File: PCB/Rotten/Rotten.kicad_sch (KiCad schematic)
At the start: 39 parts, among them J1 Jack-DC, J2 FOOTSWITCH, J3 JACK OUTPUT, J4 JACK INPUT, Q1 2N5458, U1 AS301

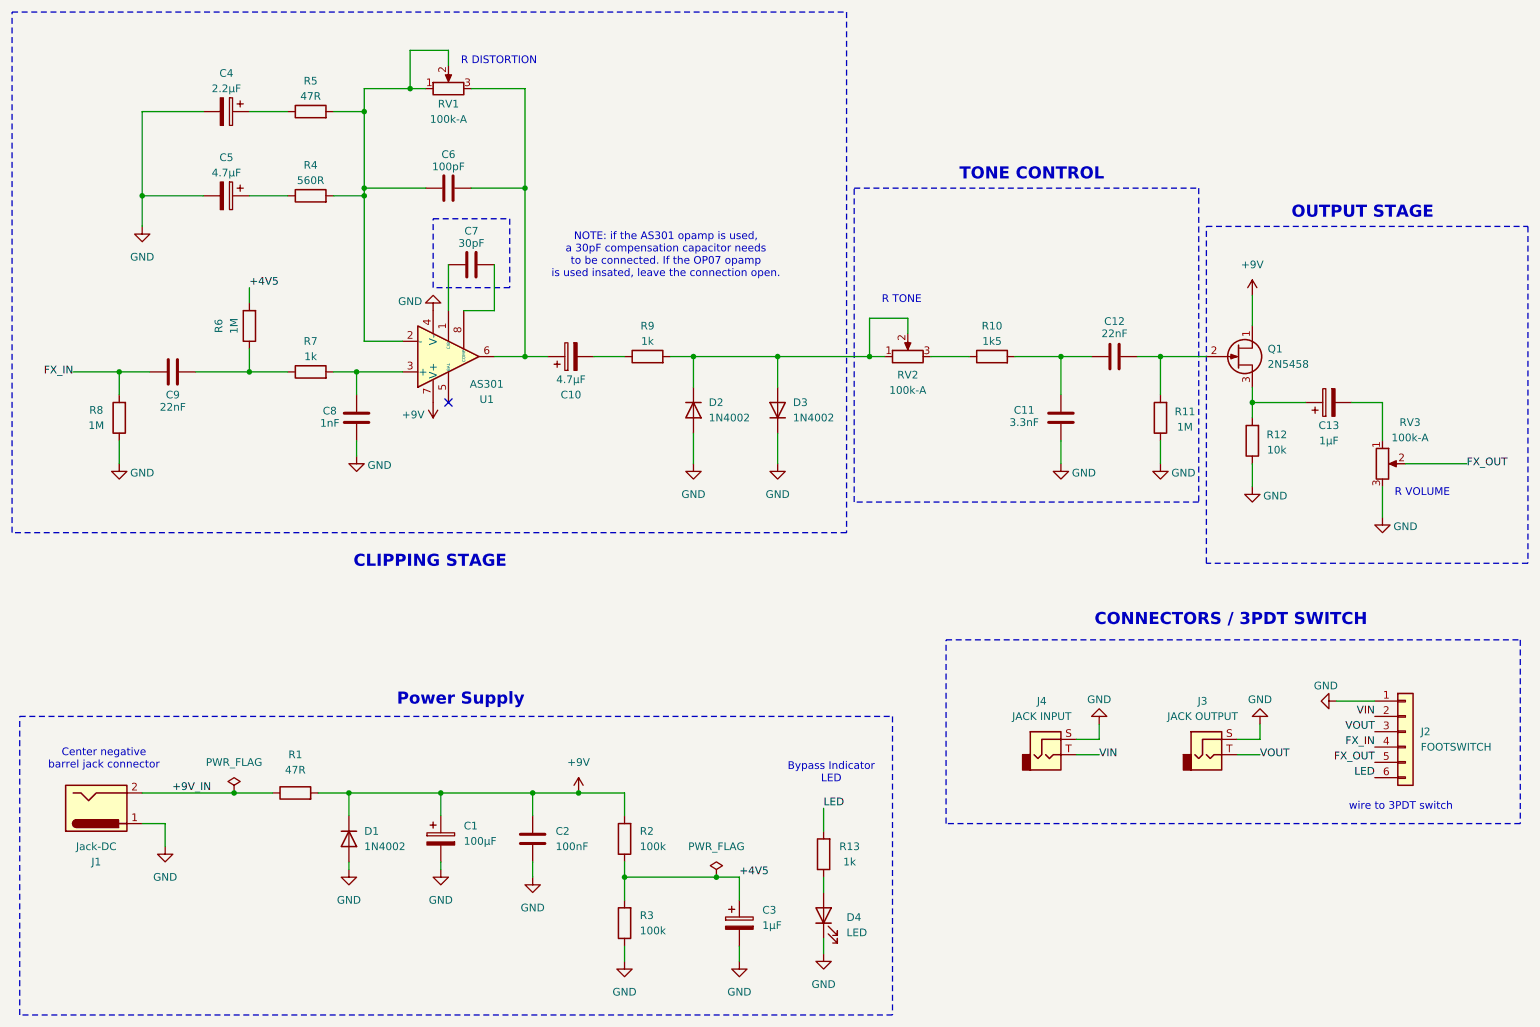
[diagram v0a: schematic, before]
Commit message: created rev1 layout and added images
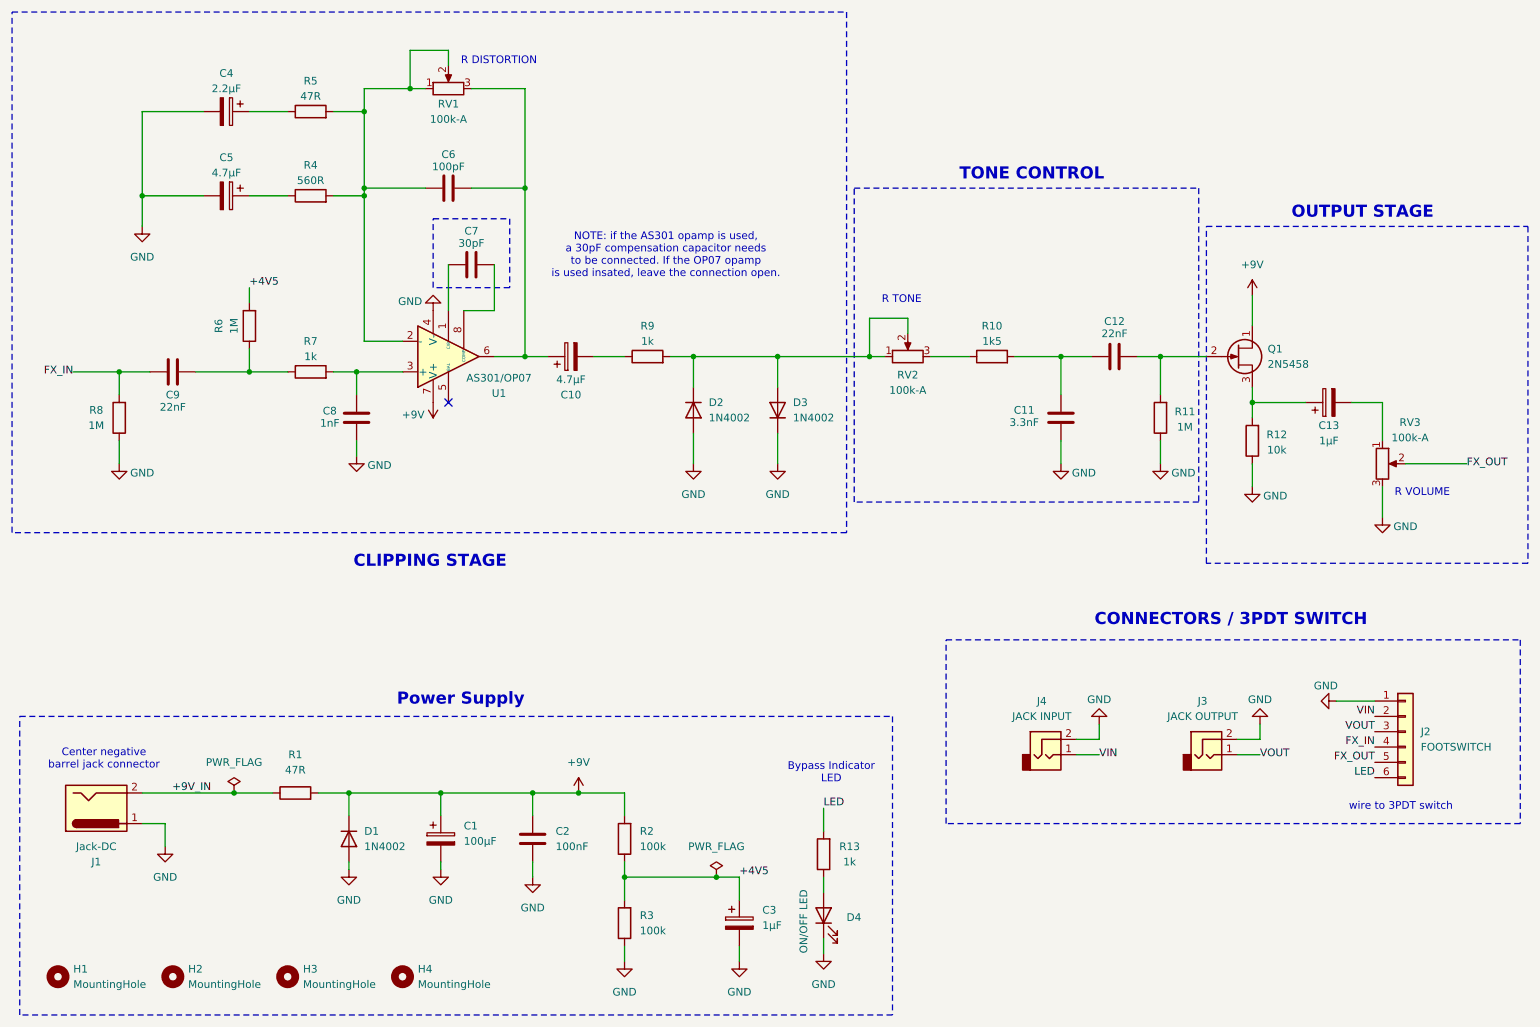
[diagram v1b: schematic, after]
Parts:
- added H1, H2, H3, H4: MountingHole, MountingHole:MountingHole_3.2mm_M3_DIN965, symbol Mechanical:MountingHole
- D4: value LED -> ON/OFF LED
- J1: footprint Connector_PinHeader_1.00mm:PinHeader_1x02_P1.00mm_Vertical -> Connector_PinHeader_2.54mm:PinHeader_1x02_P2.54mm_Vertical
- J3, J4: footprint TestPoint:TestPoint_2Pads_Pitch2.54mm_Drill0.8mm -> Connector_PinHeader_2.54mm:PinHeader_1x02_P2.54mm_Vertical
- U1: value AS301 -> AS301/OP07
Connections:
- net GND: now also J3.2, J4.2; no longer J3.S, J4.S
- net VIN: now also J4.1; no longer J4.T
- net VOUT: now also J3.1; no longer J3.T
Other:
- company: (none) -> Kromftronics
- title: (none) -> Rotten

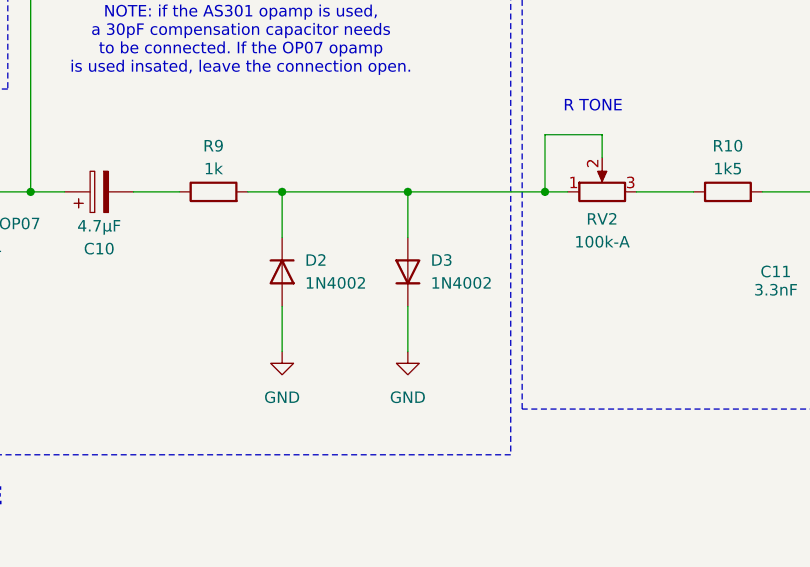
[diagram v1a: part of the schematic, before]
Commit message: changed clipping diodes to 1N4148. Updated schematic and PCB images. Generated an HTML BOM.
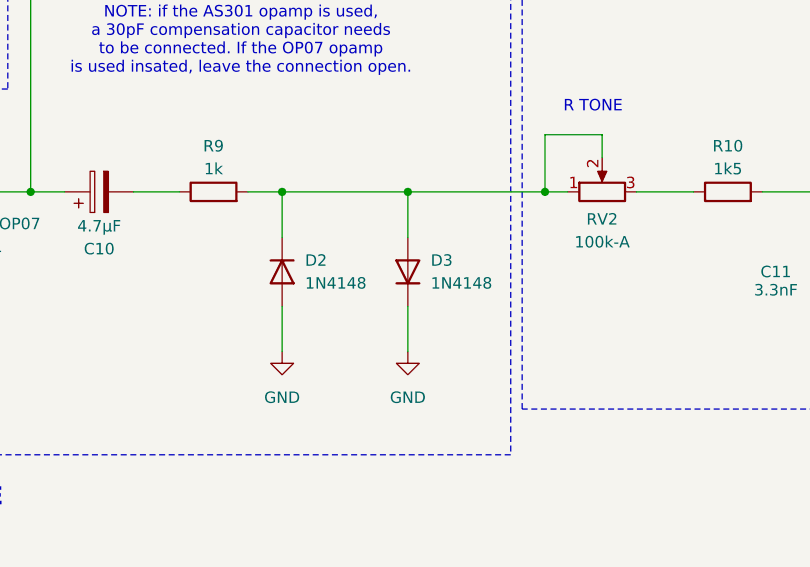
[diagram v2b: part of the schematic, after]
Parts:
- D2, D3: value 1N4002 -> 1N4148
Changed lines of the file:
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@@
 			)
 		)
-		(property "Value" "1N4002"
+		(property "Value" "1N4148"
 			(at 138.43 88.8999 90)
 			(effects
@@
 			)
 		)
-		(property "Value" "1N4002"
+		(property "Value" "1N4148"
 			(at 152.4 88.8999 90)
 			(effects

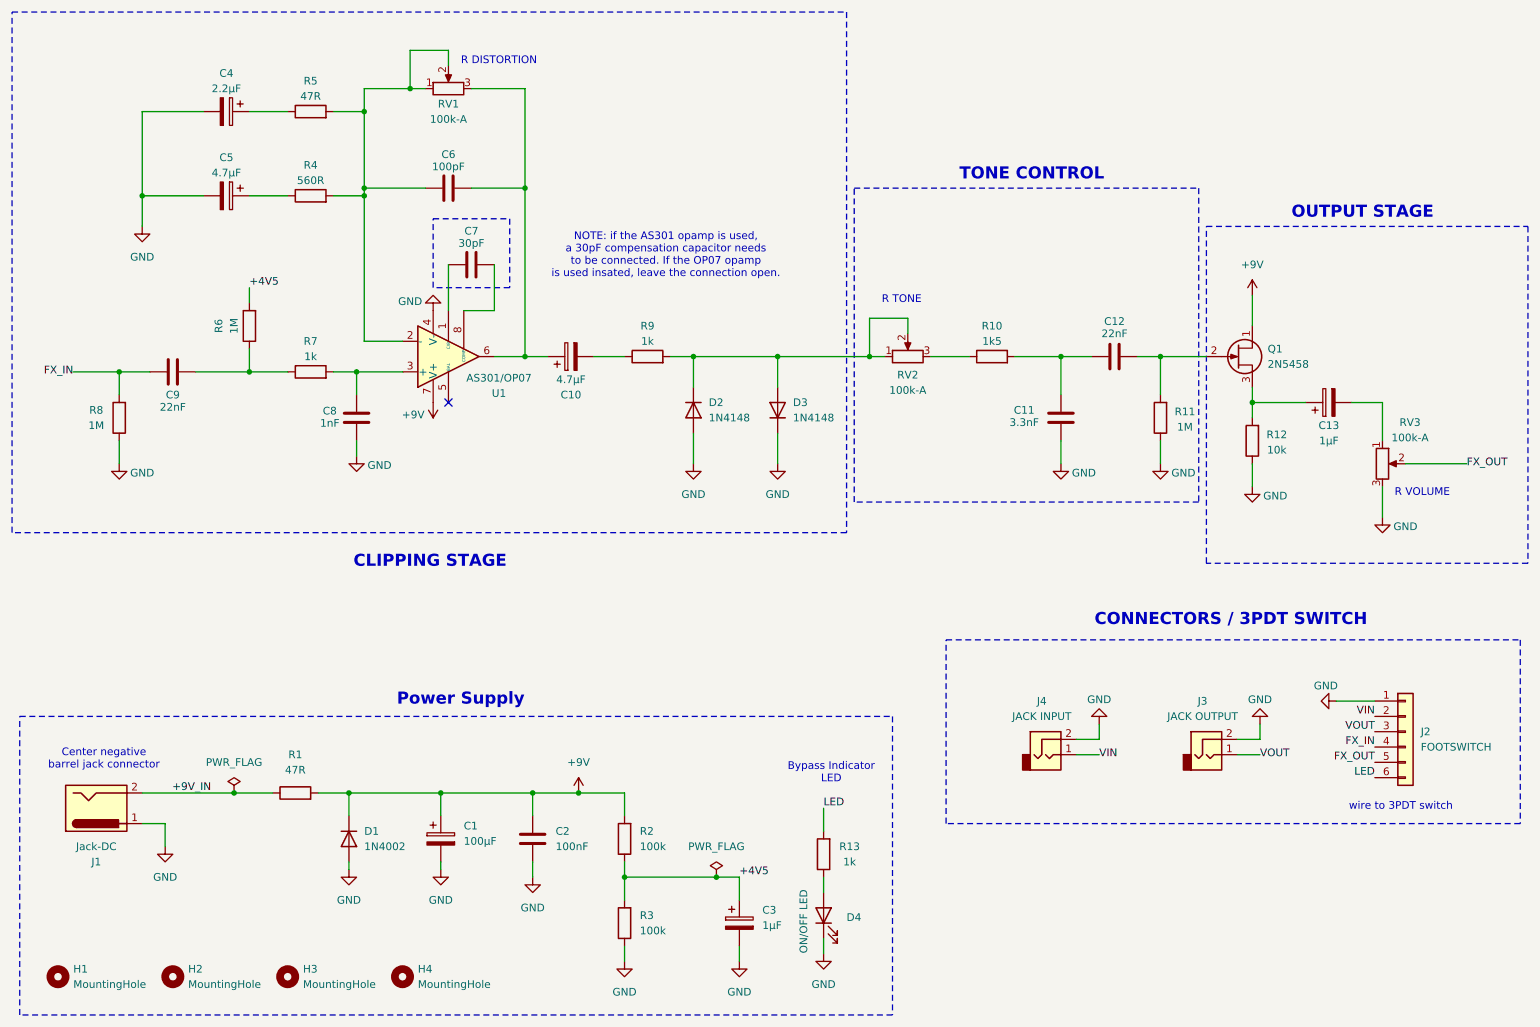
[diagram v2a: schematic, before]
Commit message: Created Rev2 update! Fixed LED footswitch error that resulted in no light. Flipped "volume" and "gain" connections on PCB (1 -> 3). Fixed wrong pinout on JFET that resulted in no audio. Updated README with new images and better build descriptions.
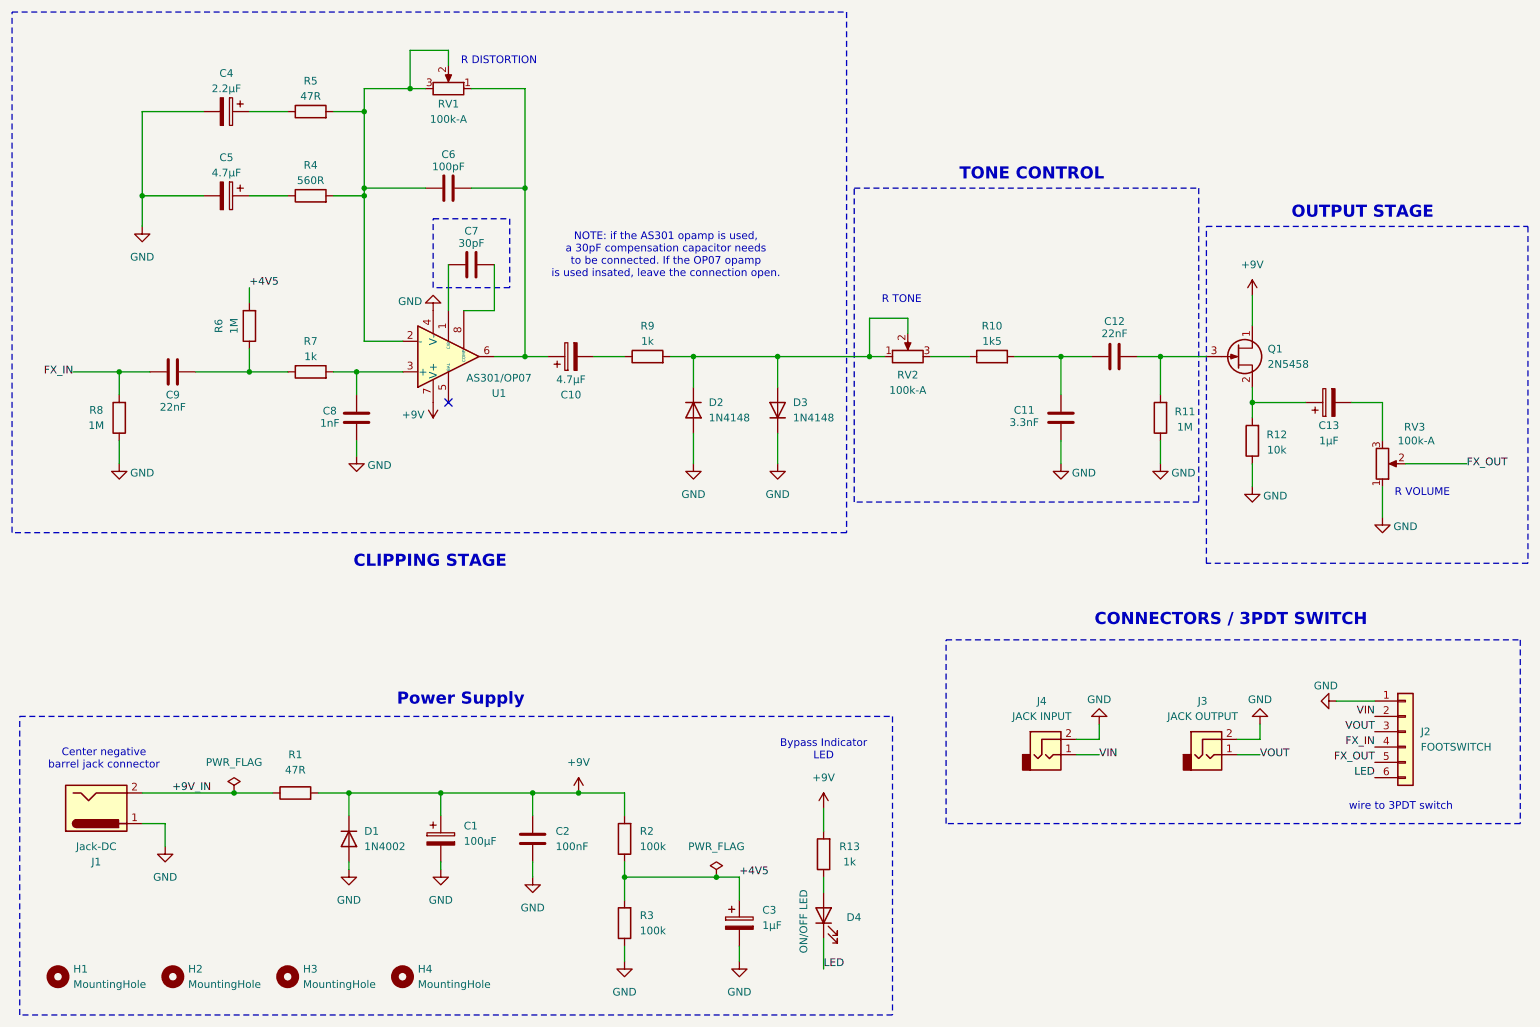
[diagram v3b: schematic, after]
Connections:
- net +9V: now also R13.2
- net GND: now also RV3.1; no longer D4.1 (K), RV3.3
- net LED: now also D4.1 (K); no longer R13.2
- net at C13.2: now also RV3.3; no longer RV3.1
- net at C13.1, R12.2: now also Q1.2 (S); no longer Q1.3 (S)
- net at C6.2, R4.2, R5.2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: now also RV1.3; no longer RV1.1
- net at C10.1, C6.1, U1.6: now also RV1.1; no longer RV1.3
- net at C12.2, R11.2: now also Q1.3 (G); no longer Q1.2 (G)
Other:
- moved on the sheet: RV1
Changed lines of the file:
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@@
 	(title_block
 		(title "Rotten")
-		(date "2024-06-06")
-		(rev "1")
+		(date "2024-10-13")
+		(rev "2")
 		(company "Kromftronics")
 	)
@@
 	(wire
 		(pts
-			(xy 157.48 175.26) (xy 157.48 177.8)
+			(xy 157.48 175.26) (xy 157.48 180.34)
 		)
 		(stroke
@@
 	(text "Bypass Indicator \nLED"
 		(exclude_from_sim no)
-		(at 158.75 147.828 0)
+		(at 157.48 144.018 0)
 		(effects
 			(font
@@
 	)
 	(label "LED"
-		(at 157.48 153.67 0)
+		(at 157.48 180.34 0)
 		(fields_autoplaced yes)
 		(effects
@@
 				(size 1.27 1.27)
 			)
-			(justify bottom)
+			(justify left bottom)
 		)
 	)
@@
 	)
 	(symbol
-		(lib_id "power:GND")
-		(at 157.48 177.8 0)
+		(lib_id "Device:R")
+		(at 185.42 78.74 90)
 		(unit 1)
 		(exclude_from_sim no)
@@
 		(on_board yes)
 		(dnp no)
-		(fields_autoplaced yes)
-		(property "Reference" "#PWR023"
-			(at 157.48 184.15 0)
+		(property "Reference" "R10"
+			(at 185.42 73.66 90)
 			(effects
 				(font
 					(size 1.27 1.27)
 				)
-				(hide yes)
 			)
 		)
-		(property "Value" "GND"
-			(at 157.48 182.88 0)
+		(property "Value" "1k5"
+			(at 185.42 76.2 90)
 			(effects
 				(font
@@
 			)
 		)
-		(property "Footprint" ""
-			(at 157.48 177.8 0)
+		(property "Footprint" "Resistor_THT:R_Axial_DIN0207_L6.3mm_D2.5mm_P7.62mm_Horizontal"
+			(at 185.42 80.518 90)
 			(effects
 				(font
@@
 			)
 		)
-		(property "Datasheet" ""
-			(at 157.48 177.8 0)
+		(property "Datasheet" "~"
+			(at 185.42 78.74 0)
 			(effects
 				(font
@@
 			)
 		)
-		(property "Description" "Power symbol creates a global label with name \"GND\" , ground"
-			(at 157.48 177.8 0)
+		(property "Description" "Resistor"
+			(at 185.42 78.74 0)
 			(effects
 				(font
@@
 		(pin "1"
 		)
+		(pin "2"
+		)
 		(instances
-			(project ""
+			(project "Rotten"
 				(path "/74bcc4c2-412b-4e26-8446-f18c8acef263"
-					(reference "#PWR023")
+					(reference "R10")
 					(unit 1)
 				)
@@
 	)
 	(symbol
-		(lib_id "Device:R")
-		(at 185.42 78.74 90)
+		(lib_id "power:+9V")
+		(at 157.48 153.67 0)
 		(unit 1)
 		(exclude_from_sim no)
@@
 		(on_board yes)
 		(dnp no)
-		(property "Reference" "R10"
-			(at 185.42 73.66 90)
+		(fields_autoplaced yes)
+		(property "Reference" "#PWR023"
+			(at 157.48 157.48 0)
 			(effects
 				(font
 					(size 1.27 1.27)
 				)
+				(hide yes)
 			)
 		)
-		(property "Value" "1k5"
-			(at 185.42 76.2 90)
+		(property "Value" "+9V"
+			(at 157.48 148.59 0)
 			(effects
 				(font
@@
 			)
 		)
-		(property "Footprint" "Resistor_THT:R_Axial_DIN0207_L6.3mm_D2.5mm_P7.62mm_Horizontal"
-			(at 185.42 80.518 90)
+		(property "Footprint" ""
+			(at 157.48 153.67 0)
 			(effects
 				(font
@@
 			)
 		)
-		(property "Datasheet" "~"
-			(at 185.42 78.74 0)
+		(property "Datasheet" ""
+			(at 157.48 153.67 0)
 			(effects
 				(font
@@
 			)
 		)
-		(property "Description" "Resistor"
-			(at 185.42 78.74 0)
+		(property "Description" "Power symbol creates a global label with name \"+9V\""
+			(at 157.48 153.67 0)
 			(effects
 				(font
@@
 		(pin "1"
 		)
-		(pin "2"
-		)
 		(instances
 			(project "Rotten"
 				(path "/74bcc4c2-412b-4e26-8446-f18c8acef263"
-					(reference "R10")
+					(reference "#PWR023")
 					(unit 1)
 				)
@@
 		(lib_id "Device:R_Potentiometer")
 		(at 250.19 96.52 0)
+		(mirror x)
 		(unit 1)
 		(exclude_from_sim no)
@@
 		(dnp no)
 		(property "Reference" "RV3"
-			(at 254.762 89.662 0)
+			(at 255.524 90.424 0)
 			(effects
 				(font
@@
 		)
 		(property "Value" "100k-A"
-			(at 254.762 92.202 0)
+			(at 255.778 92.71 0)
 			(effects
 				(font
@@
 	(symbol
 		(lib_id "Device:R_Potentiometer")
-		(at 95.25 34.29 90)
+		(at 95.25 34.29 270)
+		(mirror x)
 		(unit 1)
 		(exclude_from_sim no)
